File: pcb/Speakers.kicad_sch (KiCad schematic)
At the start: 27 parts, among them U11 ADA4511-2ARMZ, U8 NC7SB3157P6X, U9 NC7SB3157P6X

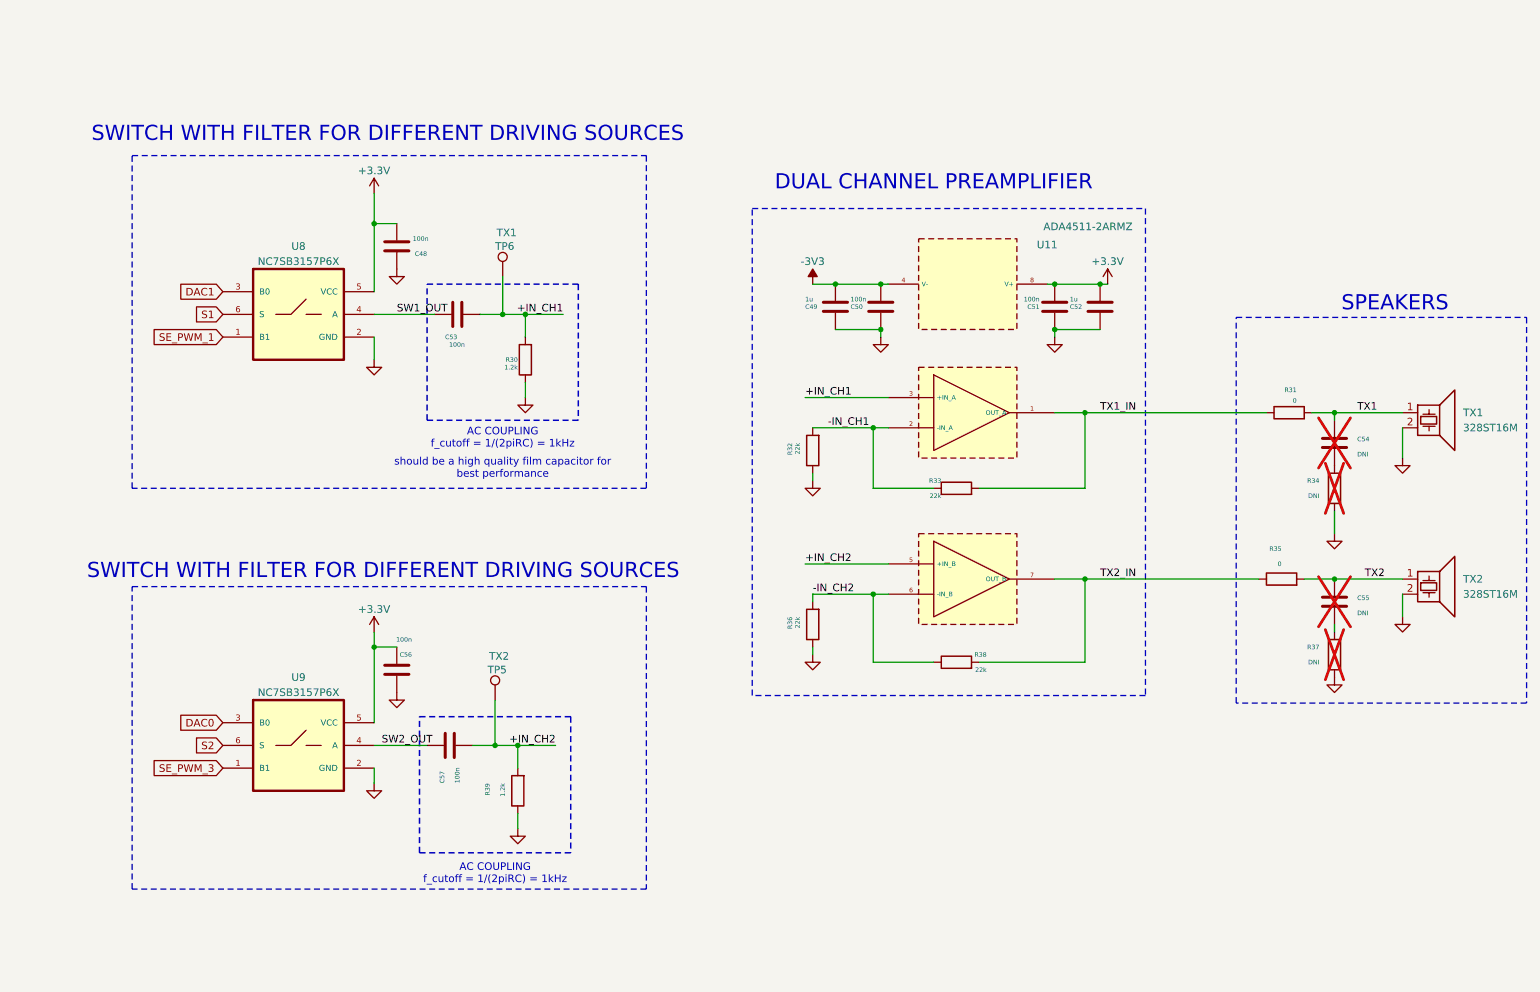
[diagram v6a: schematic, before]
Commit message: feat: Improve PCB design after tests of rev 0.8
- Added new generation of humidity sensor
- New silkscreen information for different components
- Added additional testpoints
- Removed PWM path for ultrasound transmitter
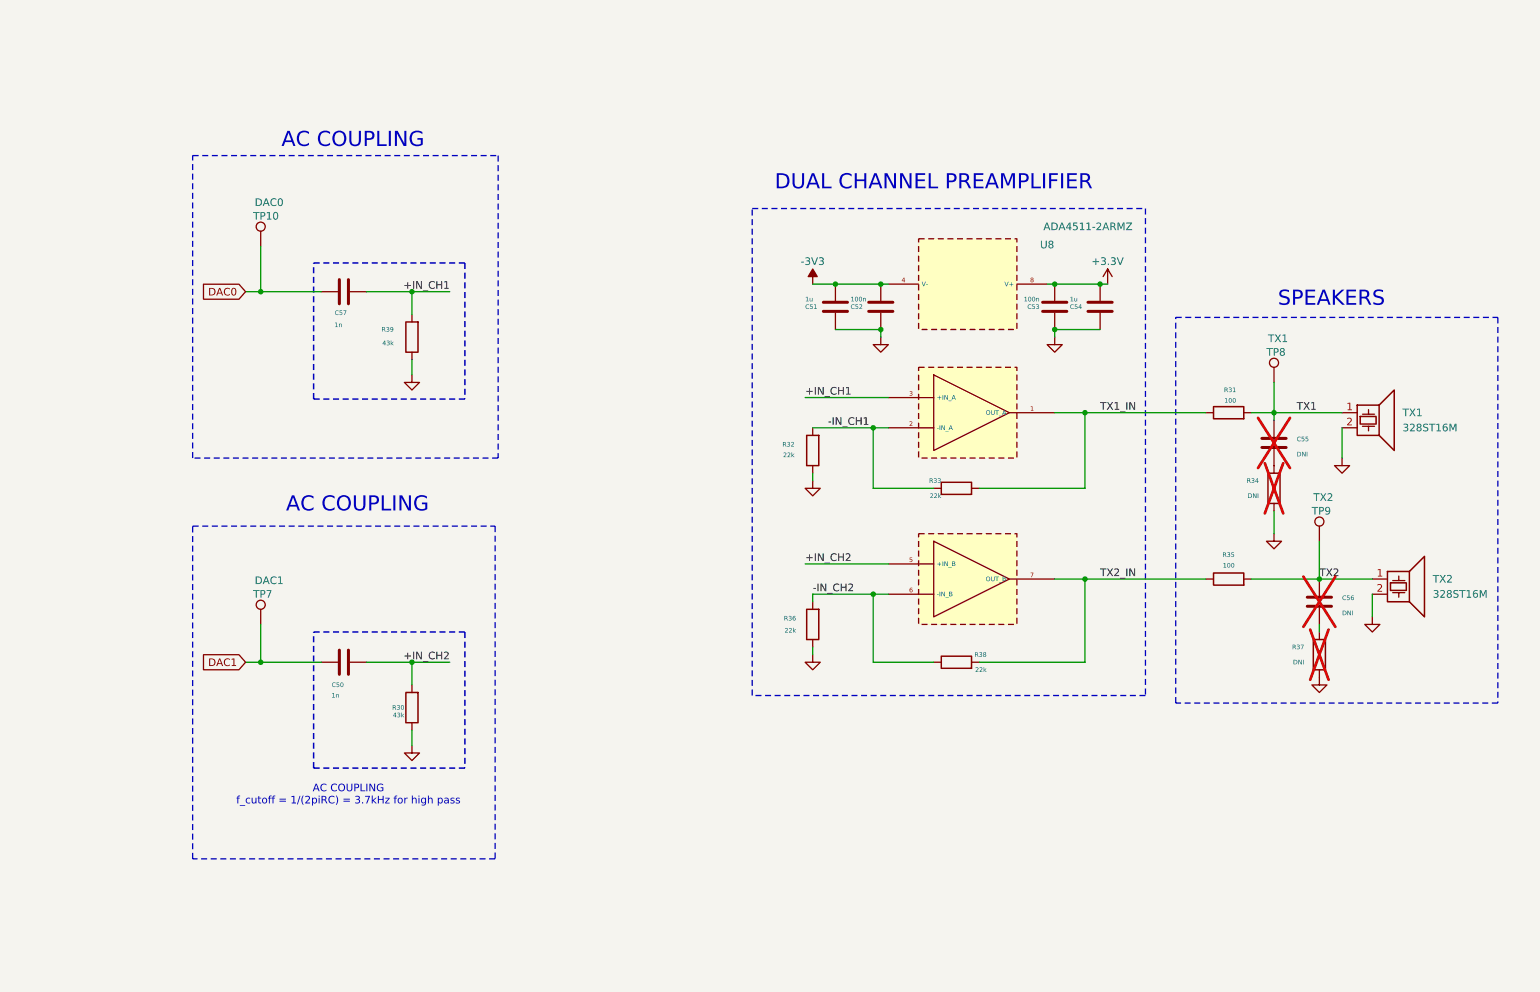
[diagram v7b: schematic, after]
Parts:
- removed C48, C56: 100n, Capacitor_SMD:C_0603_1608Metric, symbol SensEdu:C
- removed U8, U9: NC7SB3157P6X, SensEdu:SOT65P210X110-6N, symbol SensEdu:NC7SB3157P6X
- added TP10: DAC0, SensEdu:TestPoint_THTPad_D2.0mm_Drill1.0mm, symbol SensEdu:TestPoint
- added TP7: DAC1, SensEdu:TestPoint_THTPad_D2.0mm_Drill1.0mm, symbol SensEdu:TestPoint
- C50: renamed from C53; value 100n -> 1n; footprint Capacitor_SMD:C_0603_1608Metric -> SensEdu:C_0603_1608Metric
- C51: renamed from C49; footprint Capacitor_SMD:C_0603_1608Metric -> SensEdu:C_0603_1608Metric
- C52: renamed from C50; footprint Capacitor_SMD:C_0603_1608Metric -> SensEdu:C_0603_1608Metric
- C53: renamed from C51; footprint Capacitor_SMD:C_0603_1608Metric -> SensEdu:C_0603_1608Metric
- C54: renamed from C52; footprint Capacitor_SMD:C_0603_1608Metric -> SensEdu:C_0603_1608Metric
- C55: renamed from C54; footprint Capacitor_SMD:C_0603_1608Metric -> SensEdu:C_0603_1608Metric
- C56: renamed from C55; footprint Capacitor_SMD:C_0603_1608Metric -> SensEdu:C_0603_1608Metric
- C57: value 100n -> 1n; footprint Capacitor_SMD:C_0603_1608Metric -> SensEdu:C_0603_1608Metric
- R30, R39: value 1.2k -> 43k; footprint Resistor_SMD:R_0603_1608Metric -> SensEdu:R_0603_1608Metric
- R31, R35: value 0 -> 100; footprint Resistor_SMD:R_0603_1608Metric -> SensEdu:R_0603_1608Metric
- R32, R33, R34, R36, R37, R38: footprint Resistor_SMD:R_0603_1608Metric -> SensEdu:R_0603_1608Metric
- TP8: renamed from TP6; footprint TestPoint:TestPoint_THTPad_D2.0mm_Drill1.0mm -> SensEdu:TestPoint_THTPad_D2.0mm_Drill1.0mm
- TP9: renamed from TP5; footprint TestPoint:TestPoint_THTPad_D2.0mm_Drill1.0mm -> SensEdu:TestPoint_THTPad_D2.0mm_Drill1.0mm
- U8: renamed from U11; footprint SamacSys_Parts:SOP65P490X110-8N -> SensEdu:SOP65P490X110-8N
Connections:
- net SW1_OUT is gone; now on net DAC1: C50.1
- net SW2_OUT is gone; now on net DAC0: C57.1
- net +IN_CH1: now also C57.2, R39.2; no longer C50.2, R30.2, TP8.1
- net +IN_CH2: now also C50.2, R30.2; no longer C57.2, R39.2, TP9.1
- net DAC0: now also TP10.1
- net DAC1: now also TP7.1
- net TX1: now also TP8.1
- net TX2: now also TP9.1
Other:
- note added: "AC COUPLING"
- note added: "AC COUPLING f_cutoff = 1/(2piRC) = 3.7kHz for high pass"
- note removed: "AC COUPLING f_cutoff = 1/(2piRC) = 1kHz"
- note removed: "SWITCH WITH FILTER FOR DIFFERENT DRIVING SOURCES"
- note removed: "should be a high quality film capacitor for best performance"
- moved on the sheet: C50, C55, C56, C57, R30, R31, R34, R35, R37, R39, TP8, TP9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
